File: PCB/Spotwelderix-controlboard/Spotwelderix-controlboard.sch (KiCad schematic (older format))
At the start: 39 parts, among them J1 ChargerPower, J2 LEDs, J3 ExtPwr_FAn, P1 Display, P2 CONN_01X08, Q1 AO3400A, Q2 AO3400A, Q5 AO3400A, U1 NodeMCU32, U3 LM7805M_TO263

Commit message: same
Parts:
- BZ1: symbol Device:Buzzer -> Spotwelderix-controlboard-rescue:Buzzer-Device
- C1, C2, C3, C5, C6, C7, C? (x2): symbol Device:C -> Spotwelderix-controlboard-rescue:C-Device
- C4: symbol Device:CP -> Spotwelderix-controlboard-rescue:CP-Device
- H1, H2, H3, H4: symbol Mechanical:MountingHole -> Spotwelderix-controlboard-rescue:MountingHole-Mechanical
- J1: symbol Connector:Conn_01x05_Male -> Spotwelderix-controlboard-rescue:Conn_01x05_Male-Connector
- J2: symbol Connector:Conn_01x03_Male -> Spotwelderix-controlboard-rescue:Conn_01x03_Male-Connector
- P2: symbol Connector:Conn_01x09_Male -> Spotwelderix-controlboard-rescue:Conn_01x09_Male-Connector
- Q1, Q2, Q5: symbol Transistor_FET:AO3400A -> Spotwelderix-controlboard-rescue:AO3400A-Transistor_FET
- U3: symbol Regulator_Linear:LM7805_TO220 -> Spotwelderix-controlboard-rescue:LM7805_TO220-Regulator_Linear
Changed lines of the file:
@@
 $EndDescr
 $Comp
-L power:GND #PWR0101
+L Spotwelderix-controlboard-rescue:GND-power #PWR0101
 U 1 1 60253474
 P 9850 2050
@@
 $EndComp
 $Comp
-L power:+5V #PWR0102
+L Spotwelderix-controlboard-rescue:+5V-power #PWR0102
 U 1 1 60254EA9
 P 10850 1550
@@
 	9850 1900 9850 2050
 $Comp
-L Device:C C5
+L Spotwelderix-controlboard-rescue:C-Device C5
 U 1 1 60257482
 P 10400 1800
@@
 $EndComp
 $Comp
-L power:GND #PWR0103
+L Spotwelderix-controlboard-rescue:GND-power #PWR0103
 U 1 1 6025D512
 P 10400 2100
@@
 $EndComp
 $Comp
-L Device:CP C4
+L Spotwelderix-controlboard-rescue:CP-Device C4
 U 1 1 60145EA0
 P 9300 1800
@@
 	9300 1650 9300 1600
 $Comp
-L power:GND #PWR0104
+L Spotwelderix-controlboard-rescue:GND-power #PWR0104
 U 1 1 6014FA58
 P 9300 2050
@@
 	9300 1950 9300 2050
 $Comp
-L Regulator_Linear:LM7805_TO220 U3
+L Spotwelderix-controlboard-rescue:LM7805_TO220-Regulator_Linear U3
 U 1 1 602540EA
 P 9850 1600
@@
 $EndComp
 $Comp
-L power:VCC #PWR0107
+L Spotwelderix-controlboard-rescue:VCC-power #PWR0107
 U 1 1 60423BF7
 P 5850 1450
@@
 	5850 1450 5850 1550
 $Comp
-L power:GND #PWR0108
+L Spotwelderix-controlboard-rescue:GND-power #PWR0108
 U 1 1 60458421
 P 5850 2700
@@
 	9550 3600 9700 3600
 $Comp
-L power:GND #PWR0110
+L Spotwelderix-controlboard-rescue:GND-power #PWR0110
 U 1 1 604F8A60
 P 10150 3900
@@
 Shuntvoltage
 $Comp
-L power:GND #PWR0111
+L Spotwelderix-controlboard-rescue:GND-power #PWR0111
 U 1 1 601723B2
 P 9950 5500
@@
 Gate_logic
 $Comp
-L power:+5V #PWR0112
+L Spotwelderix-controlboard-rescue:+5V-power #PWR0112
 U 1 1 60233752
 P 9200 4700
@@
 	9200 4700 9200 4750
 $Comp
-L power:+5V #PWR0113
+L Spotwelderix-controlboard-rescue:+5V-power #PWR0113
 U 1 1 6018DFE6
 P 3450 2700
@@
 	3050 5550 3050 5800
 $Comp
-L power:+3V3 #PWR0114
+L Spotwelderix-controlboard-rescue:+3V3-power #PWR0114
 U 1 1 601950C4
 P 3300 2800
@@
 $EndComp
 $Comp
-L power:GND #PWR0118
+L Spotwelderix-controlboard-rescue:GND-power #PWR0118
 U 1 1 601B2294
 P 5150 2850
@@
 $EndComp
 $Comp
-L Device:C C3
+L Spotwelderix-controlboard-rescue:C-Device C3
 U 1 1 601E4B47
 P 3900 1900
@@
 $EndComp
 $Comp
-L power:GND #PWR0120
+L Spotwelderix-controlboard-rescue:GND-power #PWR0120
 U 1 1 6018CEE5
 P 3050 5900
@@
 $EndComp
 $Comp
-L power:GND #PWR0121
+L Spotwelderix-controlboard-rescue:GND-power #PWR0121
 U 1 1 601E8CEC
 P 1900 1300
@@
 $EndComp
 $Comp
-L power:GND #PWR0122
+L Spotwelderix-controlboard-rescue:GND-power #PWR0122
 U 1 1 601EC40D
 P 3900 2150
@@
 $EndComp
 $Comp
-L power:GND #PWR0123
+L Spotwelderix-controlboard-rescue:GND-power #PWR0123
 U 1 1 601EE926
 P 3250 1400
@@
 $EndComp
 $Comp
-L power:GND #PWR0124
+L Spotwelderix-controlboard-rescue:GND-power #PWR0124
 U 1 1 601F04A7
 P 4300 700
@@
 $EndComp
 $Comp
-L Device:C C2
+L Spotwelderix-controlboard-rescue:C-Device C2
 U 1 1 601F2B09
 P 3850 850
@@
 $EndComp
 $Comp
-L Device:C C1
+L Spotwelderix-controlboard-rescue:C-Device C1
 U 1 1 6020E37E
 P 1400 1850
@@
 $EndComp
 $Comp
-L power:GND #PWR0125
+L Spotwelderix-controlboard-rescue:GND-power #PWR0125
 U 1 1 6020E384
 P 1400 2100
@@
 $EndComp
 $Comp
-L power:+3V3 #PWR0130
+L Spotwelderix-controlboard-rescue:+3V3-power #PWR0130
 U 1 1 60294159
 P 5100 5100
@@
 $EndComp
 $Comp
-L power:GND #PWR0131
+L Spotwelderix-controlboard-rescue:GND-power #PWR0131
 U 1 1 6029783A
 P 4850 4900
@@
 	4250 7100 4400 7100
 $Comp
-L power:+5V #PWR0132
+L Spotwelderix-controlboard-rescue:+5V-power #PWR0132
 U 1 1 60306192
 P 4900 6450
@@
 $EndComp
 $Comp
-L power:GND #PWR0133
+L Spotwelderix-controlboard-rescue:GND-power #PWR0133
 U 1 1 603061A2
 P 4850 7400
@@
 	4850 7400 4850 7300
 $Comp
-L Device:Buzzer BZ1
+L Spotwelderix-controlboard-rescue:Buzzer-Device BZ1
 U 1 1 6031033A
 P 5550 6550
@@
 Connection ~ 9300 1600
 $Comp
-L power:PWR_FLAG #FLG0102
+L Spotwelderix-controlboard-rescue:PWR_FLAG-power #FLG0102
 U 1 1 603CC079
 P 3300 5800
@@
 	10400 1950 10400 2100
 $Comp
-L Mechanical:MountingHole H1
+L Spotwelderix-controlboard-rescue:MountingHole-Mechanical H1
 U 1 1 60212773
 P 7200 6350
@@
 $EndComp
 $Comp
-L Mechanical:MountingHole H2
+L Spotwelderix-controlboard-rescue:MountingHole-Mechanical H2
 U 1 1 602345BB
 P 8050 6350
@@
 $EndComp
 $Comp
-L Mechanical:MountingHole H3
+L Spotwelderix-controlboard-rescue:MountingHole-Mechanical H3
 U 1 1 60238BE0
 P 8900 6350
@@
 $EndComp
 $Comp
-L Mechanical:MountingHole H4
+L Spotwelderix-controlboard-rescue:MountingHole-Mechanical H4
 U 1 1 6023D34D
 P 9750 6350
@@
 	1200 4700 1400 4700
 $Comp
-L Device:C C6
+L Spotwelderix-controlboard-rescue:C-Device C6
 U 1 1 6018E2B1
 P 1400 5050
@@
 $EndComp
 $Comp
-L power:GND #PWR01
+L Spotwelderix-controlboard-rescue:GND-power #PWR01
 U 1 1 6019341A
 P 1400 5300
@@
 	1750 3700 2150 3700
 $Comp
-L Connector:Conn_01x03_Male J2
+L Spotwelderix-controlboard-rescue:Conn_01x03_Male-Connector J2
 U 1 1 6018AA6E
 P 7450 5150
@@
 $EndComp
 $Comp
-L power:GND #PWR04
+L Spotwelderix-controlboard-rescue:GND-power #PWR04
 U 1 1 60191D79
 P 6800 5150
@@
 $EndComp
 $Comp
-L power:+5V #PWR03
+L Spotwelderix-controlboard-rescue:+5V-power #PWR03
 U 1 1 60197CCB
 P 6800 5000
@@
 	1600 4400 2150 4400
 $Comp
-L power:GND #PWR05
+L Spotwelderix-controlboard-rescue:GND-power #PWR05
 U 1 1 6020A94C
 P 8300 1950
@@
 	7900 1600 8500 1600
 $Comp
-L power:PWR_FLAG #FLG01
+L Spotwelderix-controlboard-rescue:PWR_FLAG-power #FLG01
 U 1 1 602C3C21
 P 9100 5250
@@
 	8700 5250 8700 5350
 $Comp
-L power:VCC #PWR02
+L Spotwelderix-controlboard-rescue:VCC-power #PWR02
 U 1 1 602C9F87
 P 8700 5250
@@
 	9950 5450 10200 5450
 $Comp
-L Connector:Conn_01x09_Male P2
+L Spotwelderix-controlboard-rescue:Conn_01x09_Male-Connector P2
 U 1 1 6015F832
 P 10400 5050
@@
 $EndComp
 $Comp
-L Device:C C7
+L Spotwelderix-controlboard-rescue:C-Device C7
 U 1 1 60368C71
 P 8900 2850
@@
 $EndComp
 $Comp
-L power:GND #PWR013
+L Spotwelderix-controlboard-rescue:GND-power #PWR013
 U 1 1 60368C77
 P 8900 3100
@@
 	4100 4650 4300 4650
 $Comp
-L Connector:Conn_01x05_Male J1
+L Spotwelderix-controlboard-rescue:Conn_01x05_Male-Connector J1
 U 1 1 603862AC
 P 7600 2800
@@
 ChargerEna
 $Comp
-L Transistor_FET:AO3400A Q5
+L Spotwelderix-controlboard-rescue:AO3400A-Transistor_FET Q5
 U 1 1 6039FCEE
 P 10050 3600
@@
 	10150 3050 10150 3400
 $Comp
-L Transistor_FET:AO3400A Q1
+L Spotwelderix-controlboard-rescue:AO3400A-Transistor_FET Q1
 U 1 1 603B9BB1
 P 8200 3500
@@
 $EndComp
 $Comp
-L power:GND #PWR011
+L Spotwelderix-controlboard-rescue:GND-power #PWR011
 U 1 1 603C15DC
 P 8300 3800
@@
 	7800 2800 8000 2800
 $Comp
-L power:GND #PWR012
+L Spotwelderix-controlboard-rescue:GND-power #PWR012
 U 1 1 603F0AF8
 P 8500 2800
@@
 NoConn ~ 7800 3000
 $Comp
-L power:VCC #PWR014
+L Spotwelderix-controlboard-rescue:VCC-power #PWR014
 U 1 1 60466FA1
 P 9250 1100
@@
 	6300 2750 6300 2700
 $Comp
-L power:GND #PWR010
+L Spotwelderix-controlboard-rescue:GND-power #PWR010
 U 1 1 60319258
 P 6300 2750
@@
 $EndComp
 $Comp
-L Transistor_FET:AO3400A Q2
+L Spotwelderix-controlboard-rescue:AO3400A-Transistor_FET Q2
 U 1 1 604F3499
 P 4750 7100
@@
 	4400 7100 4550 7100
 $Comp
-L Device:C C?
+L Spotwelderix-controlboard-rescue:C-Device C?
 U 1 1 610D9E59
 P 4900 2450
@@
 	4850 2100 5600 2100
 $Comp
-L Device:C C?
+L Spotwelderix-controlboard-rescue:C-Device C?
 U 1 1 61115154
 P 5600 2450
@@
 6.5 kHz
 $Comp
-L power:+3V3 #PWR?
+L Spotwelderix-controlboard-rescue:+3V3-power #PWR?
 U 1 1 61125D3E
 P 4400 6600
@@
 $EndComp
 $Comp
-L power:+3V3 #PWR?
+L Spotwelderix-controlboard-rescue:+3V3-power #PWR?
 U 1 1 6112C73B
 P 9700 3050

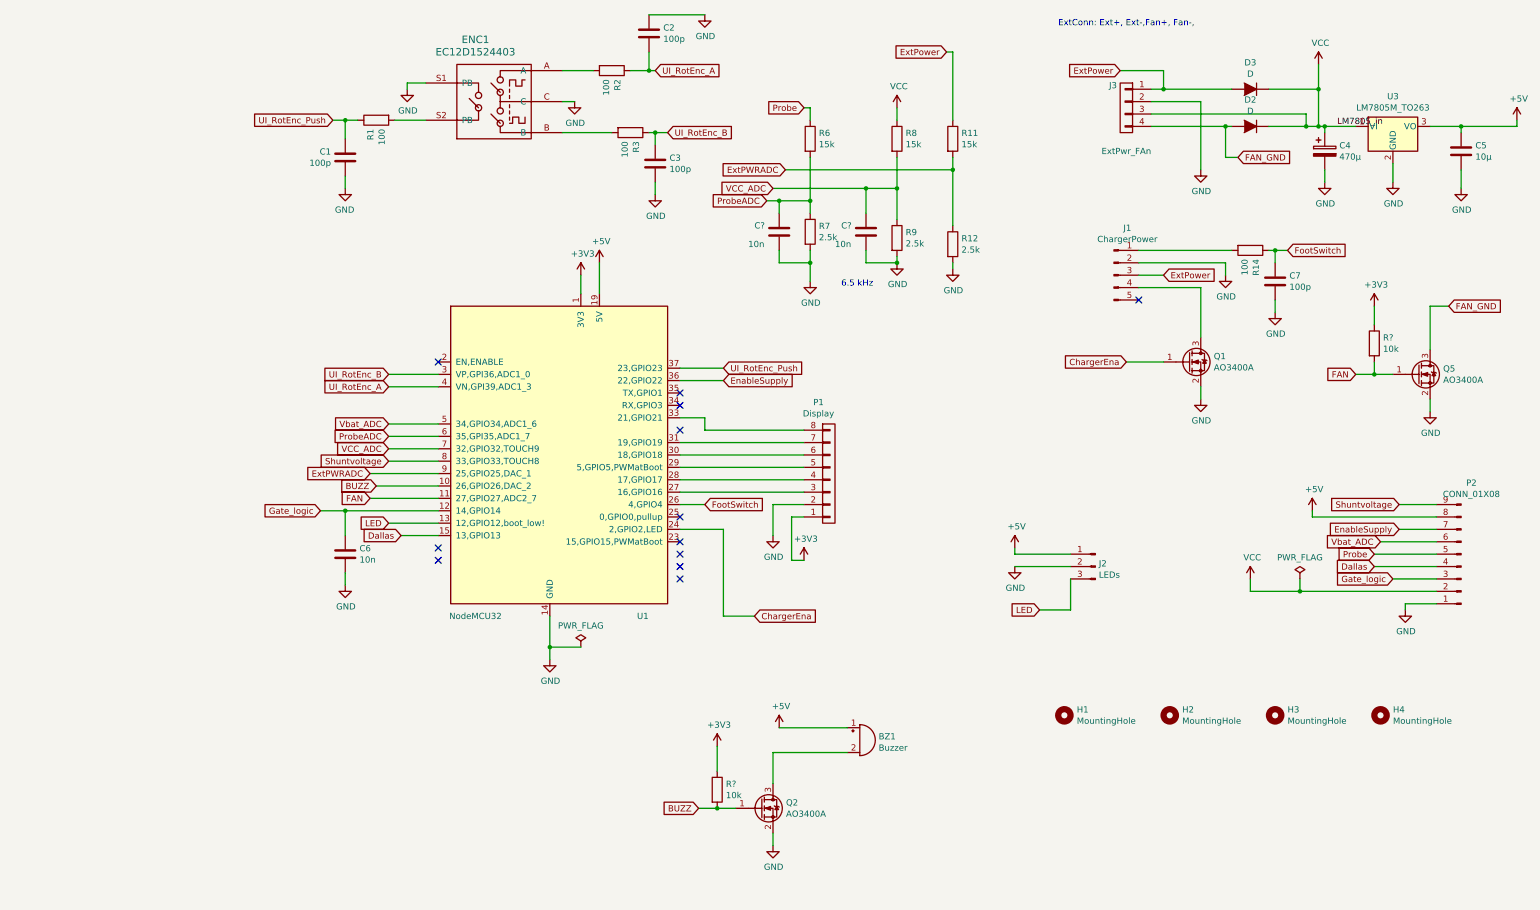
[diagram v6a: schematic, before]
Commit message: PCB v2 , Power PCB routed
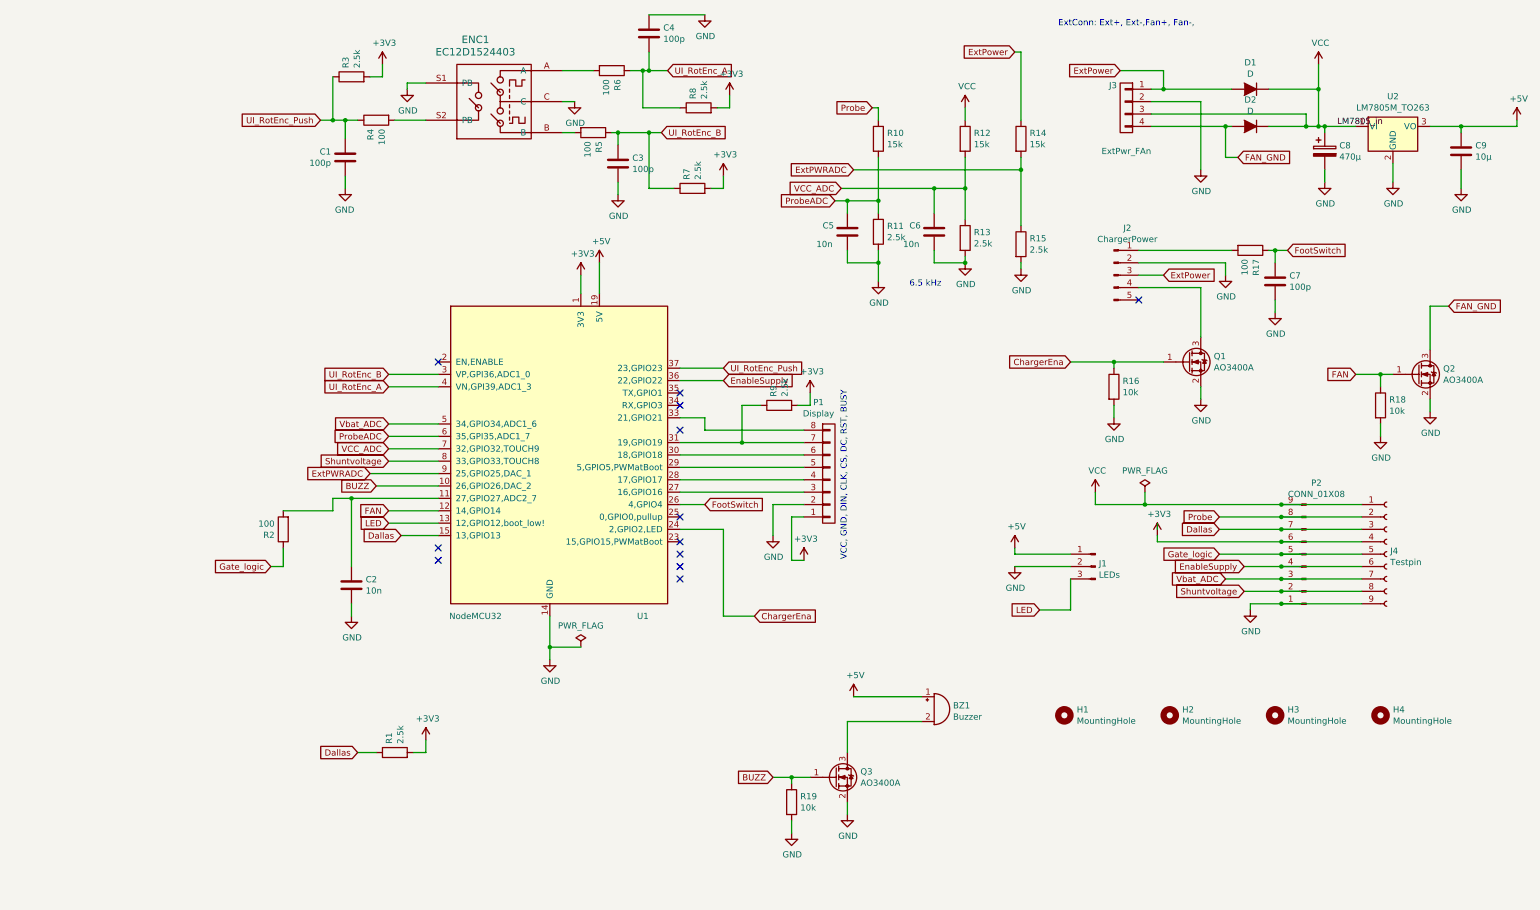
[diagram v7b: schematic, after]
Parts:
- removed R?: 10k, Resistor_SMD:R_0805_2012Metric, symbol Arduino_Spot_Welderparts:R
- added J4: Testpin, Connector_PinHeader_2.54mm:PinHeader_1x09_P2.54mm_Vertical, symbol Connector:Conn_01x09_Female
- added R1, R3, R7, R8, R9: 2.5k, Resistor_SMD:R_0805_2012Metric, symbol Arduino_Spot_Welderparts:R
- added R16, R18: 10k, Resistor_SMD:R_0805_2012Metric, symbol Arduino_Spot_Welderparts:R
- added R2: 100, Resistor_SMD:R_0805_2012Metric, symbol Arduino_Spot_Welderparts:R
- C2: renamed from C6; footprint Capacitor_SMD:C_0805_2012Metric -> Capacitor_SMD:C_1206_3216Metric_Pad1.33x1.80mm_HandSolder
- C5, C6: renamed from C?; footprint Capacitor_SMD:C_0805_2012Metric -> Capacitor_SMD:C_1206_3216Metric_Pad1.33x1.80mm_HandSolder
- C7: footprint Capacitor_SMD:C_0805_2012Metric -> Capacitor_SMD:C_1206_3216Metric_Pad1.33x1.80mm_HandSolder
- C9: renamed from C5; footprint Capacitor_SMD:C_1206_3216Metric -> Capacitor_SMD:C_1206_3216Metric_Pad1.33x1.80mm_HandSolder
- D1: renamed from D3; footprint Diode_SMD:D_SMA -> Diode_SMD:D_SMA_Handsoldering
- D2: footprint Diode_SMD:D_SMA -> Diode_SMD:D_SMA_Handsoldering
- gave numbers to parts that had none: 1
- renumbered C2 to C4, C4 to C8, J2 to J1, J1 to J2, Q5 to Q2, Q2 to Q3, R6 to R10, R7 to R11, R8 to R12, R9 to R13, R11 to R14, R12 to R15, R14 to R17, R1 to R4, R3 to R5, R2 to R6, U3 to U2
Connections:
- net +3V3: now also P2.6 (Pin_6), J4.4 (Pin_4), R1.2, R3.2, R7.2, R8.2, R9.2; no longer R19.1
- net +5V: no longer P2.8 (Pin_8)
- net BUZZ: now also R19.1; no longer R19.2
- net ChargerEna: now also R16.1
- net Dallas: now also P2.7 (Pin_7), J4.3 (Pin_3), R1.1; no longer P2.4 (Pin_4)
- net EnableSupply: now also P2.4 (Pin_4), J4.6 (Pin_6); no longer P2.7 (Pin_7)
- net FAN: now also U1.12 (14,GPIO14), R18.1; no longer U1.11 (27,GPIO27,ADC2_7)
- net GND: now also R19.2, J4.9 (Pin_9), R16.2, R18.2
- net Gate_logic: now also P2.5 (Pin_5), J4.5 (Pin_5), R2.1; no longer C2.1, P2.3 (Pin_3), U1.12 (14,GPIO14)
- net Probe: now also P2.8 (Pin_8), J4.2 (Pin_2); no longer P2.5 (Pin_5)
- net Shuntvoltage: now also P2.2 (Pin_2), J4.8 (Pin_8); no longer P2.9 (Pin_9)
- net UI_RotEnc_A: now also R8.1
- net UI_RotEnc_B: now also R7.1
- net UI_RotEnc_Push: now also R3.1
- net VCC: now also P2.9 (Pin_9), J4.1 (Pin_1); no longer P2.2 (Pin_2)
- net Vbat_ADC: now also P2.3 (Pin_3), J4.7 (Pin_7); no longer P2.6 (Pin_6)
- net at P1.7 (P7), U1.31 (19,GPIO19): now also R9.1
- new net: C2.1, R2.2, U1.11 (27,GPIO27,ADC2_7)
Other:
- note added: "VCC, GND, DIN, CLK, CS, DC, RST, BUSY\n"
- moved on the sheet: BZ1, C2, C3, C5, C6, P2, Q3, R10, R11, R12, R13, R14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

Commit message: clean up
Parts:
- removed C5: 10n, Capacitor_SMD:C_1206_3216Metric_Pad1.33x1.80mm_HandSolder, symbol Spotwelderix-controlboard-rescue:C-Device
- removed R10: 15k, Resistor_SMD:R_0805_2012Metric, symbol Arduino_Spot_Welderparts:R
- removed R11: 2.5k, Resistor_SMD:R_0805_2012Metric, symbol Arduino_Spot_Welderparts:R
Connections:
- net Probe is gone; now on net ProbeADC: J4.2 (Pin_2), P2.8 (Pin_8)
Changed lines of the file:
@@
 	1    0    0    -1
 $EndComp
-Text GLabel 8450 4750 0    50   Input ~ 0
-Probe
-$Comp
-L Arduino_Spot_Welderparts:R R10
-U 1 1 601B227D
-P 5700 1700
-F 0 "R10" H 5770 1746 50  0000 L CNN
-F 1 "15k" H 5770 1655 50  0000 L CNN
-F 2 "Resistor_SMD:R_0805_2012Metric" V 5630 1700 50  0001 C CNN
-F 3 "" H 5700 1700 50  0000 C CNN
-	1    5700 1700
-	1    0    0    -1
-$EndComp
-$Comp
-L Arduino_Spot_Welderparts:R R11
-U 1 1 601B2283
-P 5700 2450
-F 0 "R11" H 5770 2496 50  0000 L CNN
-F 1 "2.5k" H 5770 2405 50  0000 L CNN
-F 2 "Resistor_SMD:R_0805_2012Metric" H 5770 2359 50  0001 L CNN
-F 3 "" H 5700 2450 50  0001 C CNN
-	1    5700 2450
-	1    0    0    -1
-$EndComp
-$Comp
-L Spotwelderix-controlboard-rescue:GND-power #PWR017
-U 1 1 601B2294
-P 5700 2850
-F 0 "#PWR017" H 5700 2600 50  0001 C CNN
-F 1 "GND" H 5705 2677 50  0000 C CNN
-F 2 "" H 5700 2850 50  0001 C CNN
-F 3 "" H 5700 2850 50  0001 C CNN
-	1    5700 2850
-	1    0    0    -1
-$EndComp
-Wire Wire Line
-	5700 2850 5700 2700
-Text GLabel 5650 1450 0    50   Input ~ 0
-Probe
-Wire Wire Line
-	5650 1450 5700 1450
-Wire Wire Line
-	5700 1450 5700 1550
 $Comp
 L Arduino_Spot_Welderparts:CONN_01X04 J3
@@
 Wire Wire Line
 	1450 5450 1450 5550
-Text GLabel 5350 2200 0    50   Input ~ 0
-ProbeADC
-Text GLabel 5400 2100 0    50   Input ~ 0
+Text GLabel 5950 2100 0    50   Input ~ 0
 VCC_ADC
 Connection ~ 6400 2100
-Wire Wire Line
-	5350 2200 5450 2200
-Connection ~ 5700 2200
 Wire Wire Line
 	1750 3600 2150 3600
@@
 Wire Wire Line
 	6400 2100 6400 2350
-Wire Wire Line
-	5700 2200 5700 2300
 $Comp
 L Spotwelderix-controlboard-rescue:NodeMCU32-my_parts U1
@@
 	8650 5150 8950 5150
 Wire Wire Line
-	8450 4750 8950 4750
+	8550 4750 8950 4750
 Wire Wire Line
 	8450 5050 8950 5050
@@
 Text GLabel 8650 5150 0    50   Input ~ 0
 EnableSupply
-Wire Wire Line
-	5700 1850 5700 2200
 Text GLabel 8500 5250 0    50   Input ~ 0
 Vbat_ADC
@@
 Text GLabel 6800 1000 0    50   Input ~ 0
 ExtPower
-Text GLabel 5500 1950 0    50   Input ~ 0
+Text GLabel 6150 1950 0    50   Input ~ 0
 ExtPWRADC
 Wire Wire Line
@@
 Wire Wire Line
 	5000 6850 5150 6850
-$Comp
-L Spotwelderix-controlboard-rescue:C-Device C5
-U 1 1 610D9E59
-P 5450 2450
-F 0 "C5" H 5250 2500 50  0000 L CNN
-F 1 "10n" H 5200 2350 50  0000 L CNN
-F 2 "Capacitor_SMD:C_1206_3216Metric_Pad1.33x1.80mm_HandSolder" H 5488 2300 50  0001 C CNN
-F 3 "https://www.mouser.de/ProductDetail/Samsung-Electro-Mechanics/CL31A106KBHNNNE/?qs=sGAEpiMZZMuMW9TJLBQkXpvci%252BYHLlg21rnqFxf28Ww%3D" H 5450 2450 50  0001 C CNN
-	1    5450 2450
-	1    0    0    -1
-$EndComp
-Wire Wire Line
-	5450 2300 5450 2200
-Connection ~ 5450 2200
-Wire Wire Line
-	5450 2200 5700 2200
-Wire Wire Line
-	5450 2600 5450 2700
-Wire Wire Line
-	5450 2700 5700 2700
-Connection ~ 5700 2700
-Wire Wire Line
-	5700 2700 5700 2600
-Wire Wire Line
-	5500 1950 6850 1950
-Wire Wire Line
-	5400 2100 6150 2100
+Wire Wire Line
+	6150 1950 6850 1950
+Wire Wire Line
+	5950 2100 6150 2100
 $Comp
 L Spotwelderix-controlboard-rescue:C-Device C6
@@
 Wire Wire Line
 	900  4700 1300 4700
+Text GLabel 8550 4750 0    50   Input ~ 0
+ProbeADC
 $EndSCHEMATC
